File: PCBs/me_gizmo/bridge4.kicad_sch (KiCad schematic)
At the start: 16 parts, among them J1 Conn_01x02_Pin, J3 Conn_01x06_Pin

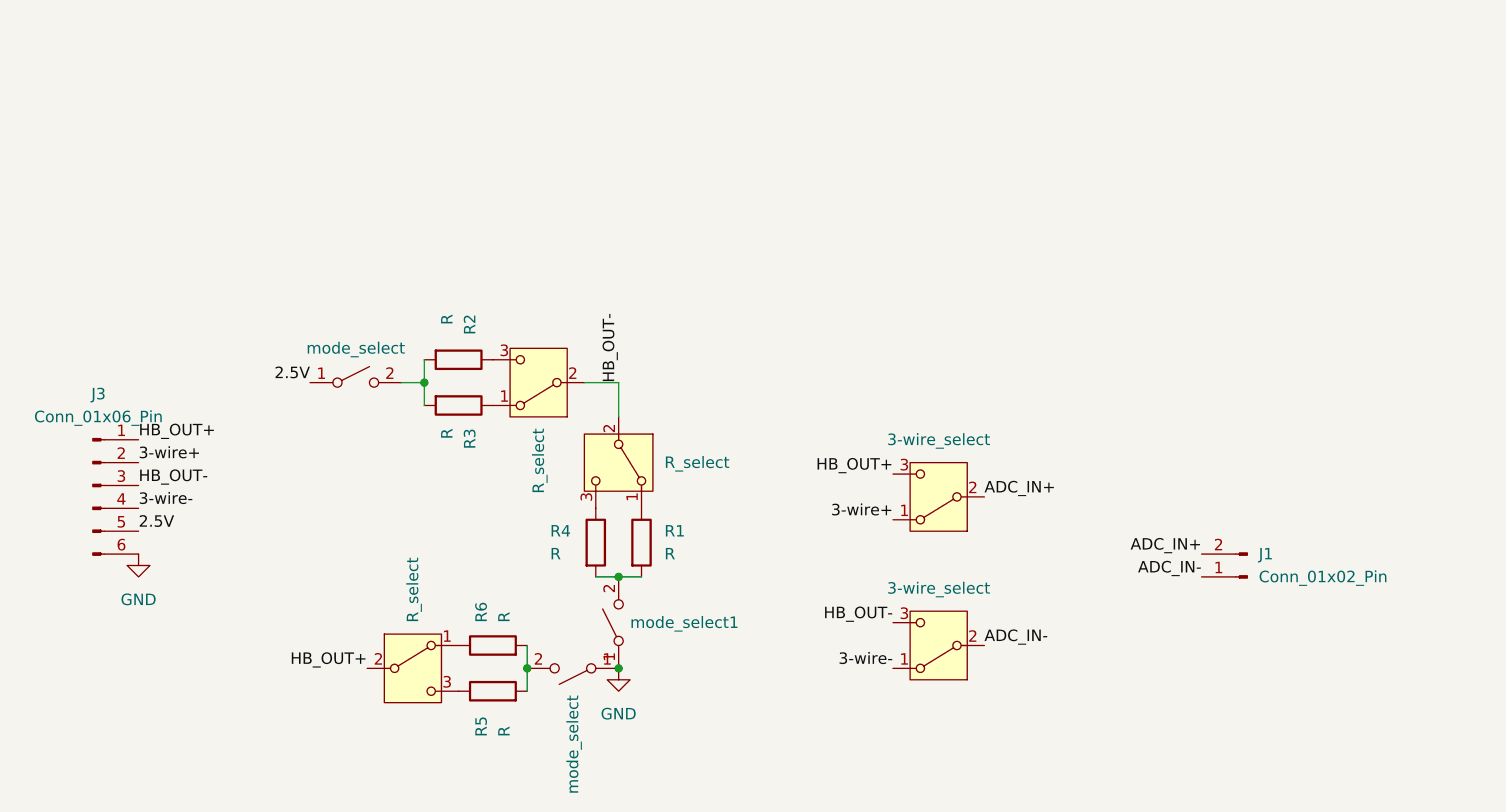
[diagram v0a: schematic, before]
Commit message: Collection script that utilizes the streaming feature for 4-channel ADC and kicad schematic for wheatstone bridge breakout board
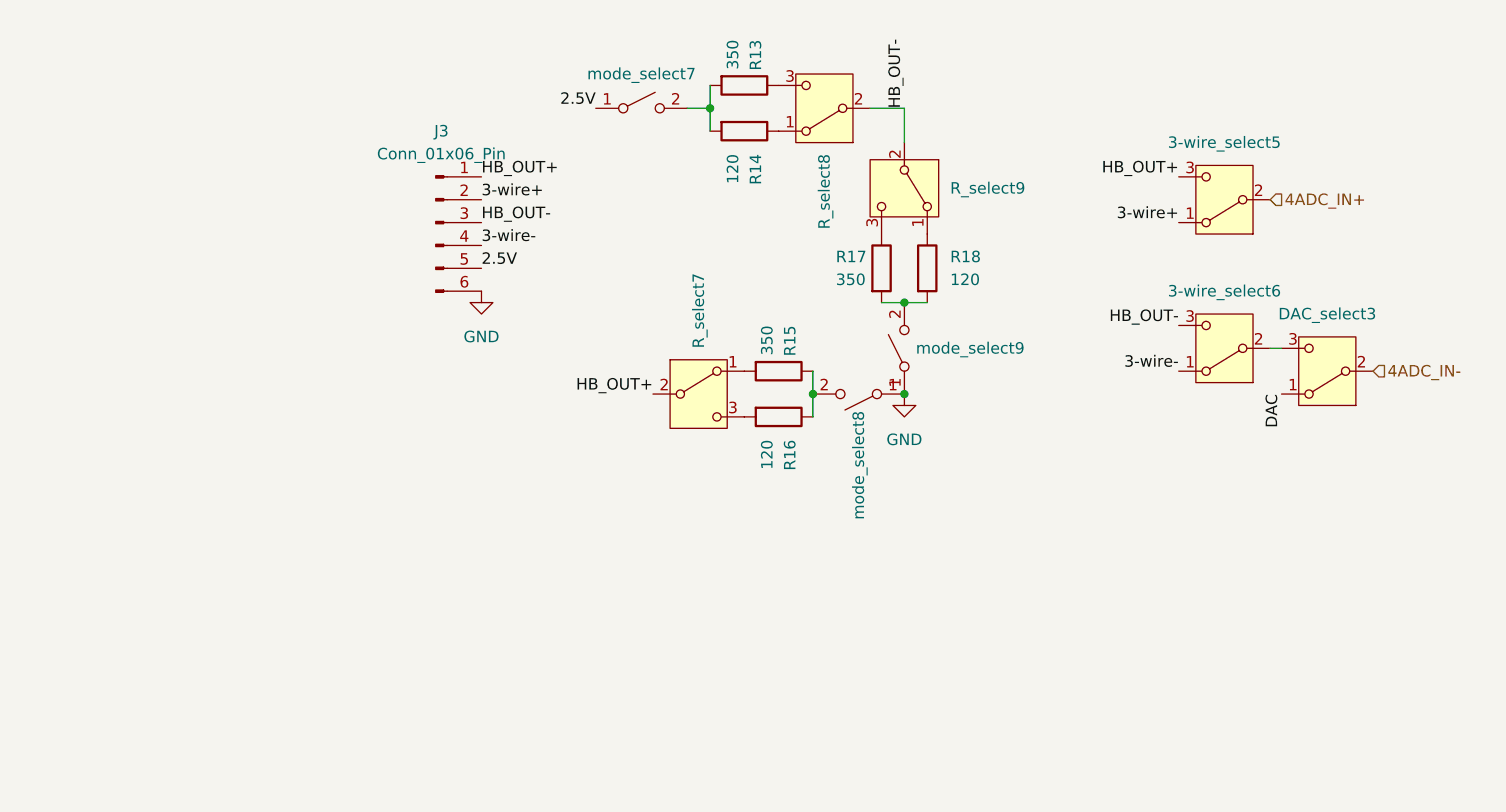
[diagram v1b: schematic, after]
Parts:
- removed 3-wire_select (x2), R_select (x3): SW_SPDT, symbol Switch:SW_SPDT
- removed J1: Conn_01x02_Pin, symbol Connector:Conn_01x02_Pin
- removed R1, R2, R3, R4, R5, R6: R, symbol Device:R
- removed mode_select (x2), mode_select1: SW_SPST, symbol Switch:SW_SPST
- added 3-wire_select5, 3-wire_select6, DAC_select3, R_select7, R_select8, R_select9: SW_SPDT, symbol Switch:SW_SPDT
- added R13, R15, R17: 350, symbol Device:R
- added R14, R16, R18: 120, symbol Device:R
- added mode_select7, mode_select8, mode_select9: SW_SPST, symbol Switch:SW_SPST
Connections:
- net 2.5V: now also mode_select7.1 (A)
- net 3-wire+: now also 3-wire_select5.1 (A)
- net 3-wire-: now also 3-wire_select6.1 (A)
- net GND: now also mode_select8.1 (A), mode_select9.1 (A)
- net HB_OUT+: now also 3-wire_select5.3 (C), R_select7.2 (B)
- net HB_OUT-: now also 3-wire_select6.3 (C), R_select8.2 (B), R_select9.2 (B)
- new net: R18.1, R_select9.1 (A)
- new net: R17.1, R_select9.3 (C)
- new net: 3-wire_select6.2 (B), DAC_select3.3 (C)
- new net: R15.1, R16.1, mode_select8.2 (B)
- new net: R13.2, R14.2, mode_select7.2 (B)
- new net: R16.2, R_select7.3 (C)
- new net: R14.1, R_select8.1 (A)
- new net: R13.1, R_select8.3 (C)
- new net: R17.2, R18.2, mode_select9.2 (B)
- new net: R15.2, R_select7.1 (A)
- new net 4ADC_IN+: 3-wire_select5.2 (B)
- new net 4ADC_IN-: DAC_select3.2 (B)
- new net DAC: DAC_select3.1 (A)
